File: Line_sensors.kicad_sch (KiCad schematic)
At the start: 0 parts

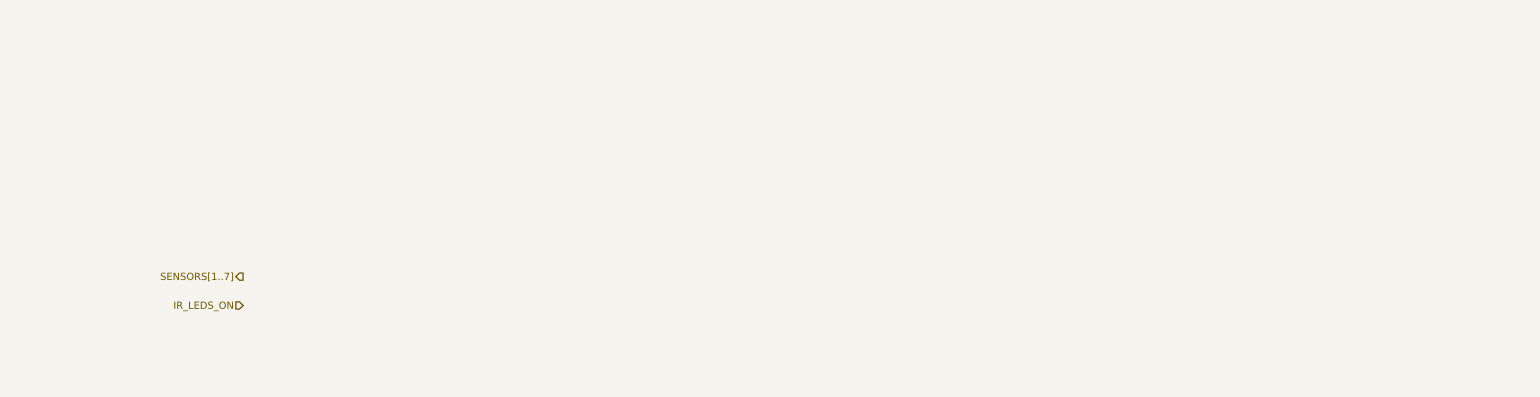
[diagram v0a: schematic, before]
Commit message: Line sensors
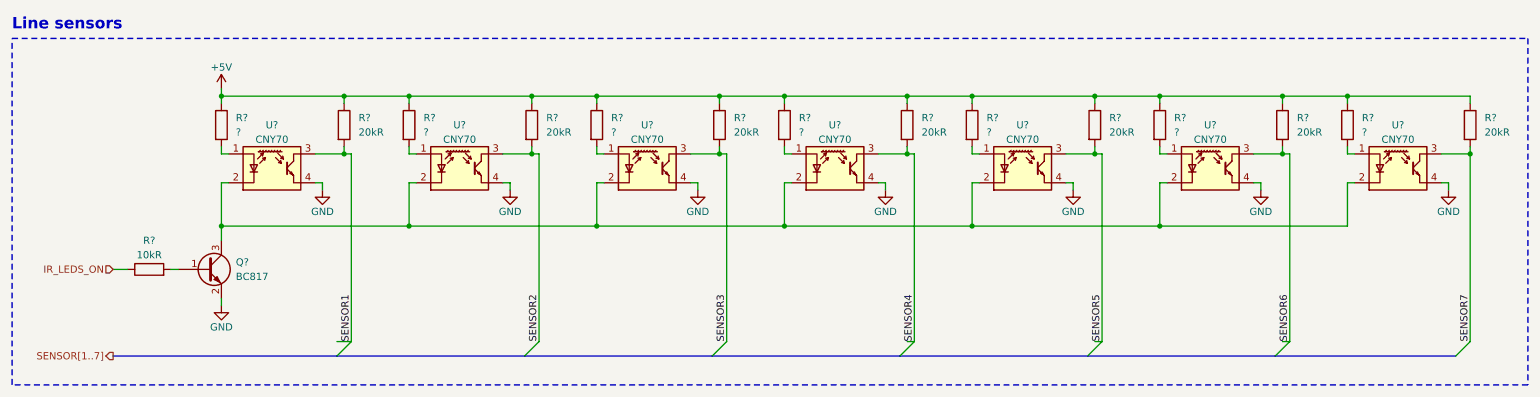
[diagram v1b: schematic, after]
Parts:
- added Q?: BC817, Package_TO_SOT_SMD:SOT-23, symbol Transistor_BJT:BC817
- added R?: 10kR, symbol Device:R
- added R? (x7): ?, symbol Device:R
- added R? (x7): 20kR, symbol Device:R
- added U? (x7): CNY70, OptoDevice:Vishay_CNY70, symbol Sensor_Proximity:CNY70
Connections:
- net IR_LEDS_ON: now also R?.1
- new net: Q?.1 (B), R?.2
- new net: R?.2, U?.1 (A) (x7)
- new net: Q?.3 (C), U?.2 (K), U?.2 (K), U?.2 (K), U?.2 (K), U?.2 (K), U?.2 (K), U?.2 (K)
- new net +5V: R?.1, R?.1, R?.1, R?.1, R?.1, R?.1, R?.1, R?.1, R?.1, R?.1, R?.1, R?.1, R?.1, R?.1
- new net GND: Q?.2 (E), U?.4 (E), U?.4 (E), U?.4 (E), U?.4 (E), U?.4 (E), U?.4 (E), U?.4 (E)
- new net SENSOR1: R?.2, U?.3 (C)
- new net SENSOR2: R?.2, U?.3 (C)
- new net SENSOR3: R?.2, U?.3 (C)
- new net SENSOR4: R?.2, U?.3 (C)
- new net SENSOR5: R?.2, U?.3 (C)
- new net SENSOR6: R?.2, U?.3 (C)
- new net SENSOR7: R?.2, U?.3 (C)
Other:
- note added: "Line sensors"

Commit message: Annotate schematics
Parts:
- gave numbers to parts that had none: 23
